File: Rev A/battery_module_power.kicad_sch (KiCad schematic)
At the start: 0 parts

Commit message: Added buck converter schematic.
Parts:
- added C1: 1uF, symbol Device:C
- added C2: 25uF, symbol Device:C
- added C3: 1000uF, symbol Device:C
- added D1, D2: 1N5819WS, Diode_SMD:D_SOD-323, symbol Diode:1N5819WS
- added D3: LED Green, LED_SMD:LED_0805_2012Metric, symbol Device:LED_Small
- added F1: 12A, symbol Device:Fuse
- added L1: 480uH, symbol Device:L
- added Q1: IRLZ44N, Package_TO_SOT_THT:TO-220-3_Vertical, symbol Transistor_FET:IRLZ44N
- added R1: 1K, symbol Device:R
- added R2: 100K, symbol Device:R
- added R3: 620, symbol Device:R
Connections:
- new net: C2.1, F1.1, L1.2, R3.1
- new net: D3.2 (A), R3.2
- new net: C3.1, D2.1 (K), Q1.2 (D)
- new net: C1.1, Q1.1 (G), R1.1, R2.2
- new net: D1.1 (K), L1.1, Q1.3 (S)
- new net BatteryModuleVin: D2.2 (A)
- new net BuckConverterHighSideSwitch: R1.2
- new net GND: C1.2, C2.2, C3.2, D1.2 (A), D3.1 (K), R2.1
- new net VBattery: F1.2

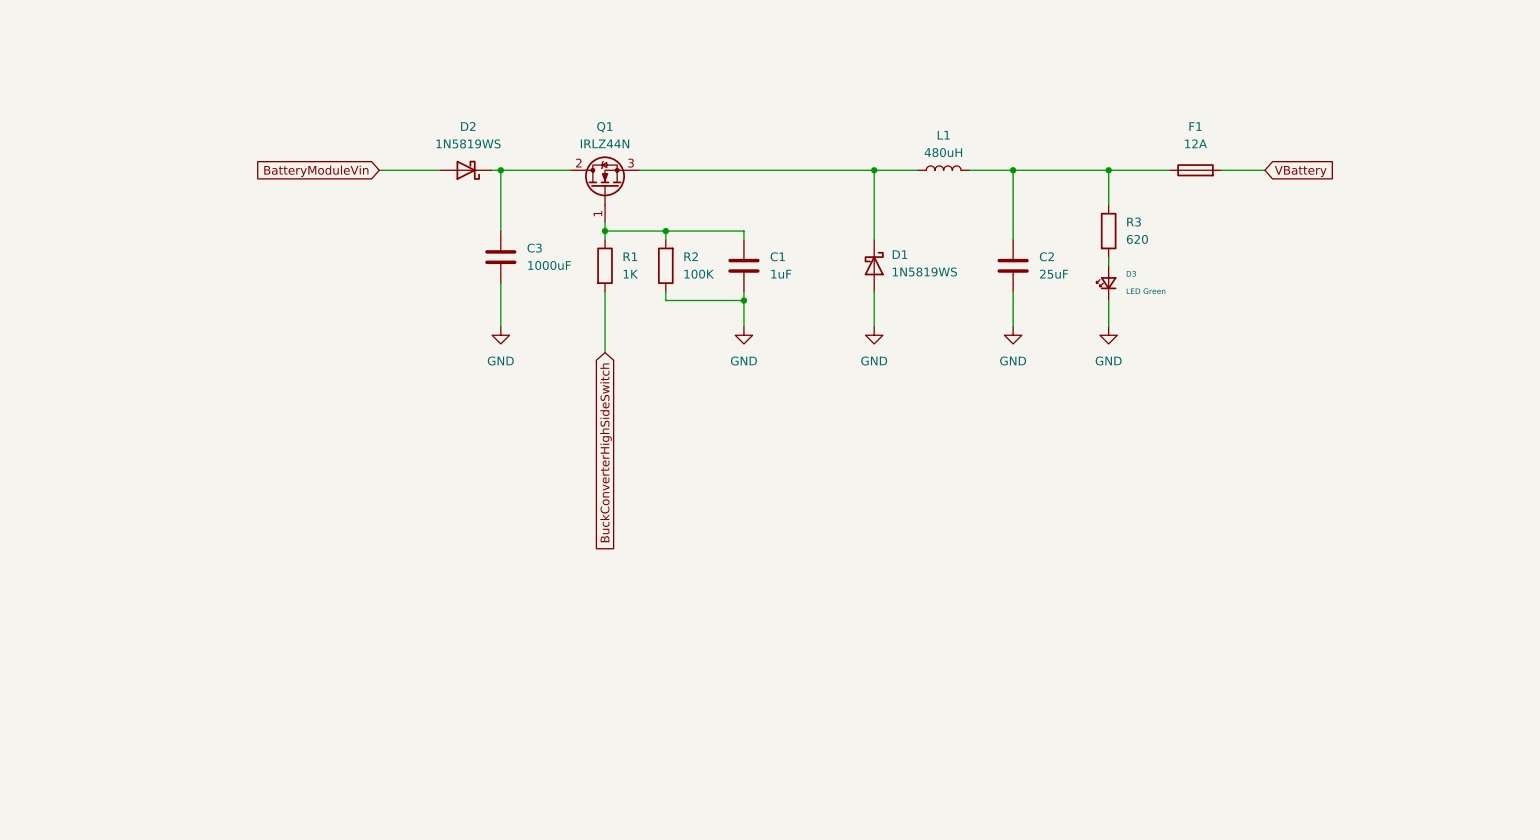
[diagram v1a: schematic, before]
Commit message: Used push-pull BJT circuit to drive MOSFET.
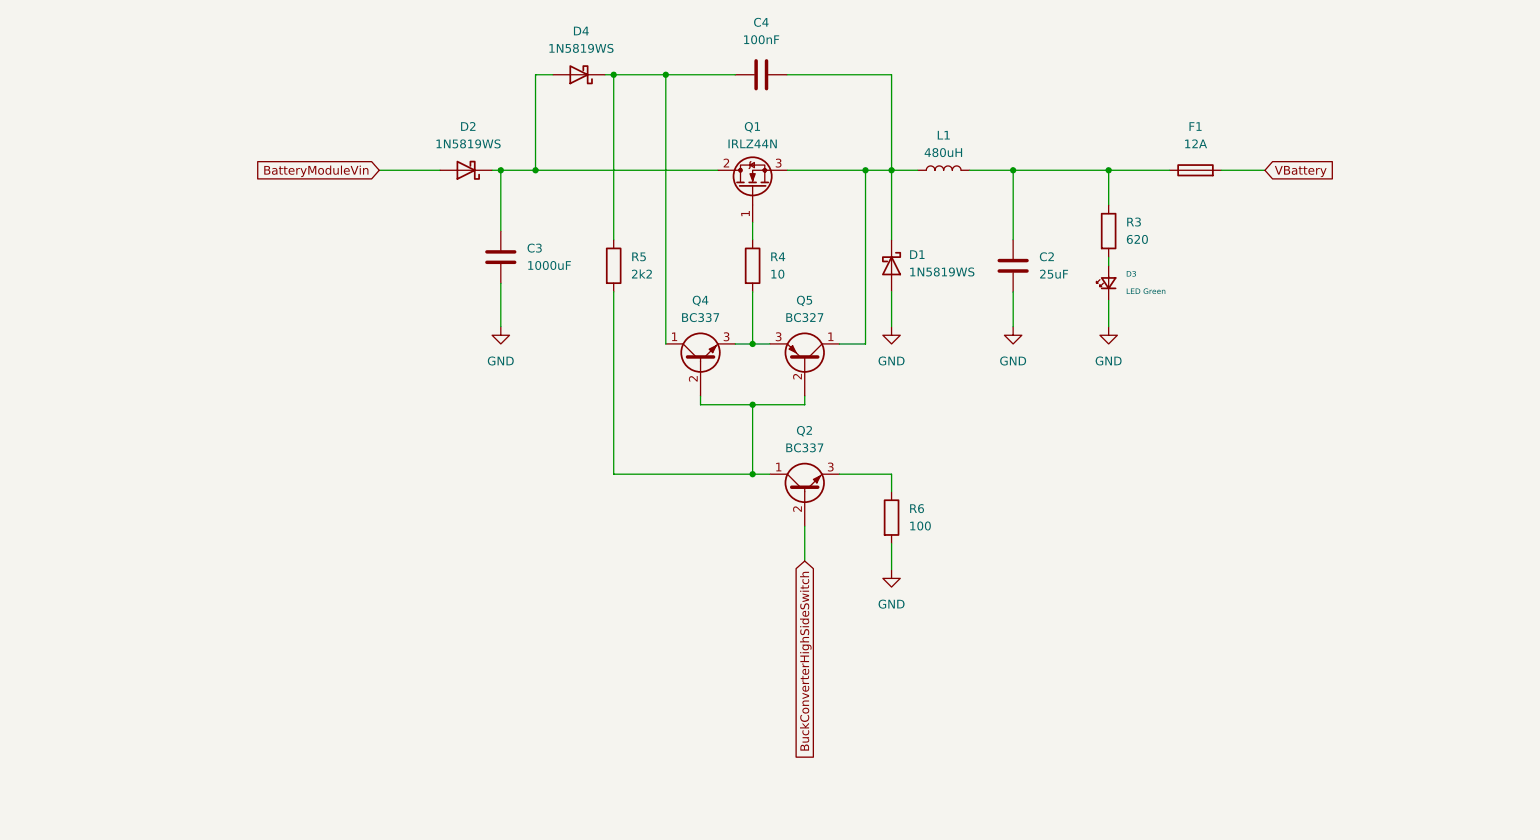
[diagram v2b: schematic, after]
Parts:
- removed C1: 1uF, symbol Device:C
- removed R1: 1K, symbol Device:R
- removed R2: 100K, symbol Device:R
- added C4: 100nF, symbol Device:C
- added D4: 1N5819WS, Diode_SMD:D_SOD-323, symbol Diode:1N5819WS
- added Q2, Q4: BC337, Package_TO_SOT_THT:TO-92_Inline, symbol Transistor_BJT:BC337
- added Q5: BC327, Package_TO_SOT_THT:TO-92_Inline, symbol Transistor_BJT:BC327
- added R4: 10, symbol Device:R
- added R5: 2k2, symbol Device:R
- added R6: 100, symbol Device:R
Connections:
- net BuckConverterHighSideSwitch: now also Q2.2 (B)
- net GND: now also R6.2
- net at C3.1, D2.1 (K), Q1.2 (D): now also D4.2 (A)
- net at Q1.1 (G): now also R4.1
- net at D1.1 (K), L1.1, Q1.3 (S): now also C4.2, Q5.1 (C)
- new net: Q2.1 (C), Q4.2 (B), Q5.2 (B), R5.2
- new net: Q2.3 (E), R6.1
- new net: C4.1, D4.1 (K), Q4.1 (C), R5.1
- new net: Q4.3 (E), Q5.3 (E), R4.2
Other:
- moved on the sheet: D1, Q1

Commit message: Updated buck.
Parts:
- removed D1, D2, D4: 1N5819WS, Diode_SMD:D_SOD-323, symbol Diode:1N5819WS
- removed Q2: BC337, Package_TO_SOT_THT:TO-92_Inline, symbol Transistor_BJT:BC337
- removed R6: 100, symbol Device:R
- added C1: 470uF, symbol Device:C
- added C7, C8: 0.1uF, Capacitor_SMD:C_0805_2012Metric, symbol Device:C
- added D1: SZSMF4L15CAT3G, Diode_SMD:D_SOD-123F, symbol Device:D_TVS
- added D2, D7, D8: PMEG045V150EPD, Package_TO_SOT_SMD:Nexperia_CFP15_SOT-1289, symbol Diode:PMEG045V150EPD
- added Q6: IRLZ44N, Package_TO_SOT_THT:TO-220-3_Vertical, symbol Transistor_FET:IRLZ44N
- C2: value 25uF -> 22uF
- C3: value 1000uF -> 470uF
- C4: value 100nF -> 0.1uF; footprint (none) -> Capacitor_SMD:C_0805_2012Metric
- L1: value 480uH -> 100uH 10.5A
- R3: value 620 -> 1K; footprint (none) -> Resistor_SMD:R_0805_2012Metric
- R4: value 10 -> 5; footprint (none) -> Resistor_SMD:R_0805_2012Metric
- R5: footprint (none) -> Resistor_SMD:R_0805_2012Metric
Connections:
- net BatteryModuleVin: now also D7.1 (A), D7.2 (A)
- net BuckConverterHighSideSwitch: now also Q4.2 (B), Q5.2 (B), R5.2
- net GND: now also C1.2, C7.2, C8.2, D1.1 (A1), D2.1 (A), D2.2 (A)
- net VBattery: now also R3.1
- net at C2.1, F1.1, L1.2: now also C8.1, D1.2 (A2); no longer R3.1
- net at C4.1, Q4.1 (C), R5.1: now also D8.3 (K)
- net at C3.1, Q1.2 (D): now also C1.1, C7.1, D7.3 (K), D8.1 (A), D8.2 (A), Q6.2 (D)
- net at C4.2, L1.1, Q1.3 (S)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: now also D2.3 (K), Q6.3 (S)
- net at Q1.1 (G), R4.1: now also Q6.1 (G)
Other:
- moved on the sheet: C2, C3, C4, D3, F1, L1, Q1, Q4, Q5, R3, R4, R5
